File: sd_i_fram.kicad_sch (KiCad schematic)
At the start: 11 parts, among them J1 Conn_02x05, J2 Micro_SD_Card

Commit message: Add files via upload
Jeszcze PCB
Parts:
- removed J1: Conn_02x05, symbol Connector_Generic:Conn_02x05_Counter_Clockwise
- added J5: Conn_02x05_Odd_Even, symbol Connector_Generic:Conn_02x05_Odd_Even
- C10: renamed from C5; value 100n -> 100nF
- C9: renamed from C7; value 100n -> 100nF
- J6: renamed from J2; value Micro_SD_Card -> Goodram M1AA microSD 16GB 100MB/s UHS-I klasa 10 z adapterem
- renumbered FRAM2 to FRAM1, R11 to R3, R12 to R4, R13 to R5, R9 to R6, R8 to R7, R10 to R8
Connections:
- net GND_CPU: now also J5.3 (Pin_3), J5.5 (Pin_5), J5.7 (Pin_7), J5.9 (Pin_9)
- net MISO: now also J5.4 (Pin_4)
- net MOSI: now also J5.2 (Pin_2)
- net SCK: now also J5.6 (Pin_6)
- net VDD: now also J5.1 (Pin_1)
- net FRAM CS renamed #FRAM CS
- net #FRAM CS: now also J5.10 (Pin_10)
- net SD CS renamed #SD CS
- net #SD CS: now also J5.8 (Pin_8)

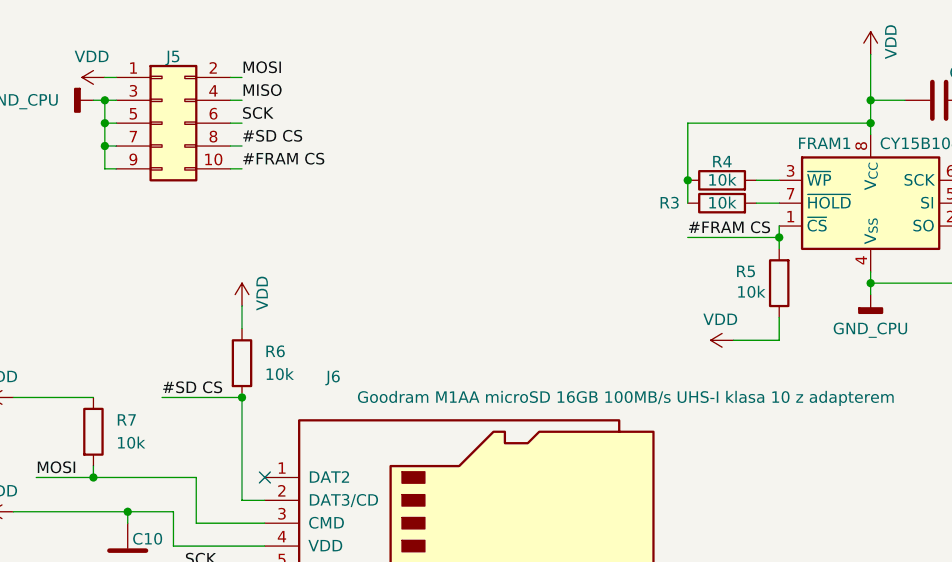
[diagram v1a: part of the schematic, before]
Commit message: poprawki po 'pracy' michala na schemacie. Poprawione PCB pamieci po Kubie. Grubsze sciezki, poprawiona pozycja decoupling capacitora
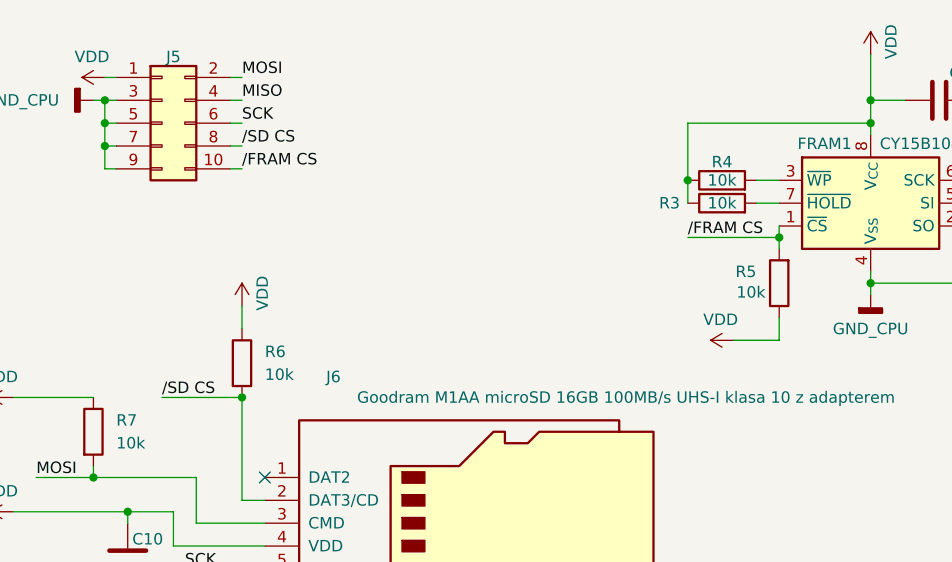
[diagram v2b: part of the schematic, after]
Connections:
- net #FRAM CS renamed /FRAM CS
- net #SD CS renamed /SD CS
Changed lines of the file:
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@@
 		)
 	)
-	(label "#FRAM CS"
+	(label "{slash}FRAM CS"
 		(at 59.69 44.45 0)
 		(effects
@@
 		)
 	)
-	(label "#SD CS"
+	(label "{slash}SD CS"
 		(at 50.8 69.85 0)
 		(effects
@@
 		)
 	)
-	(label "#SD CS"
+	(label "{slash}SD CS"
 		(at 59.69 41.91 0)
 		(effects
@@
 		)
 	)
-	(label "#FRAM CS"
+	(label "{slash}FRAM CS"
 		(at 109.22 52.07 0)
 		(effects

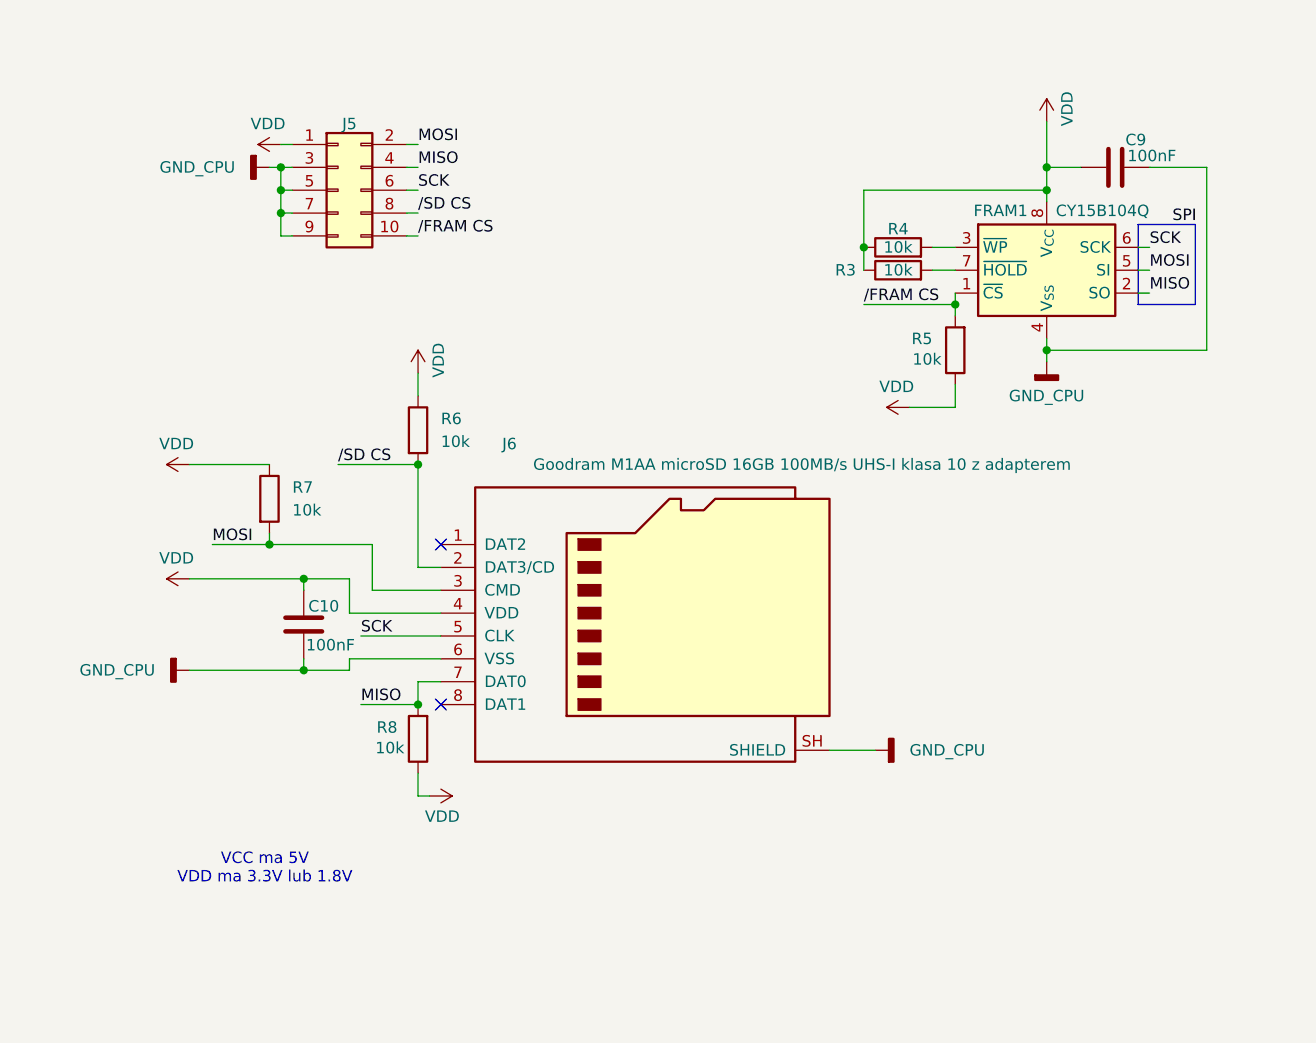
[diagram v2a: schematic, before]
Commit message: dodane footprinty
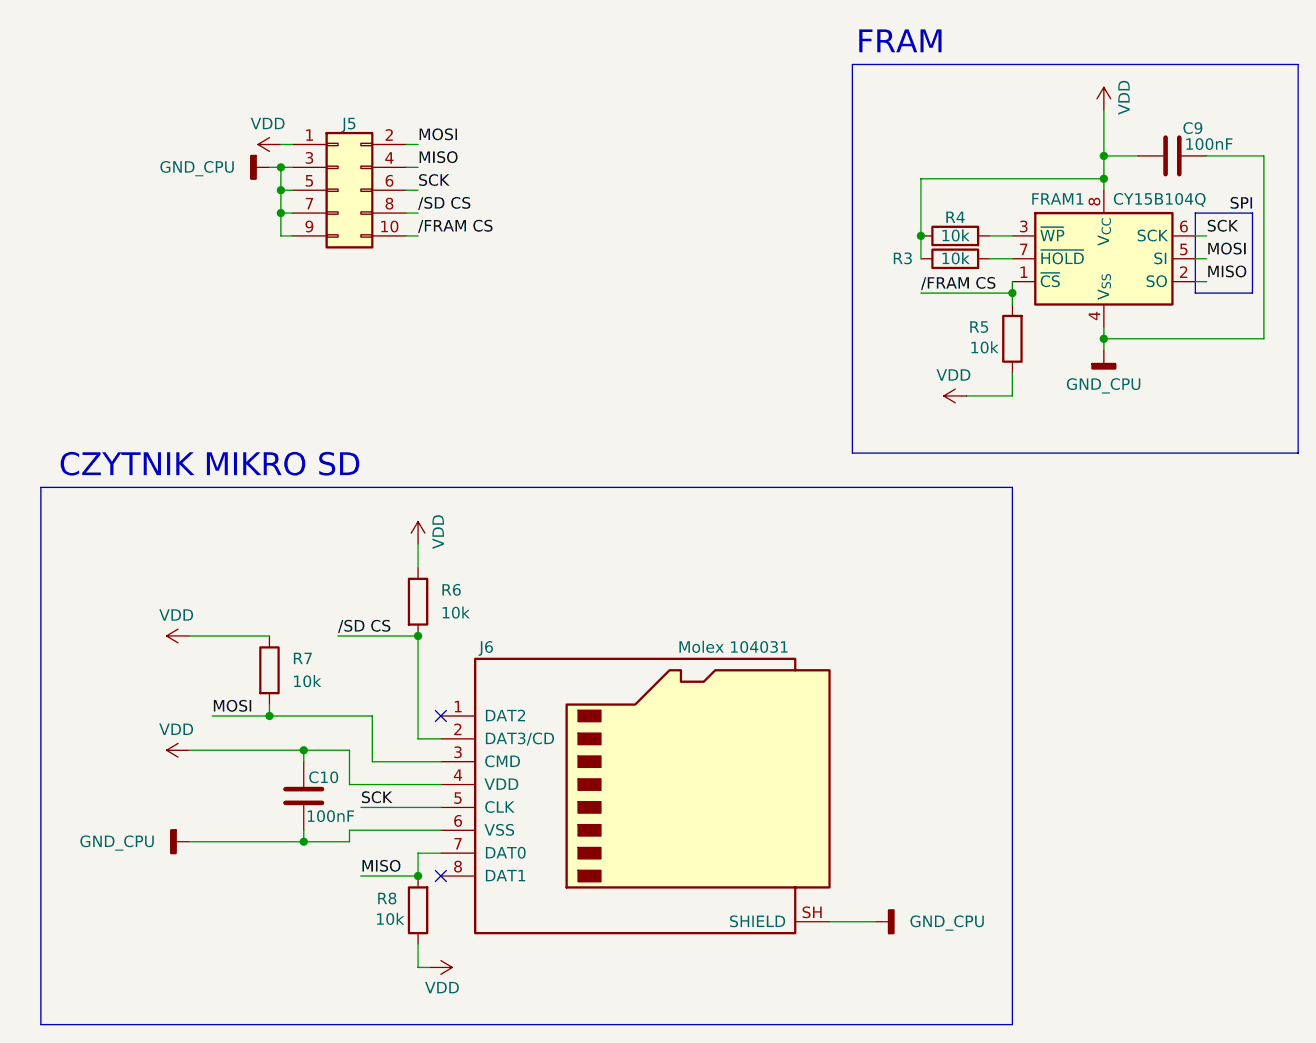
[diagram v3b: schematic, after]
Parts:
- C10, C9: footprint (none) -> Capacitor_SMD:C_0805_2012Metric
- J5: footprint (none) -> Connector_PinHeader_2.54mm:PinHeader_2x06_P2.54mm_Vertical
- J6: value Goodram M1AA microSD 16GB 100MB/s UHS-I klasa 10 z adapterem -> Molex 104031; footprint (none) -> Connector_Card:microSD_HC_Hirose_DM3D-SF
- R3, R4, R5, R6, R7, R8: footprint (none) -> Resistor_SMD:R_0805_2012Metric
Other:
- note added: "CZYTNIK MIKRO SD"
- note added: "FRAM"
- note removed: "VCC ma 5V VDD ma 3.3V lub 1.8V"
- moved on the sheet: C10, C9, FRAM1, J6, R3, R4, R5, R6, R7, R8
